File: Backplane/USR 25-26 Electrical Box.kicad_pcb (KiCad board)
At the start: 2 copper layers, 3 parts

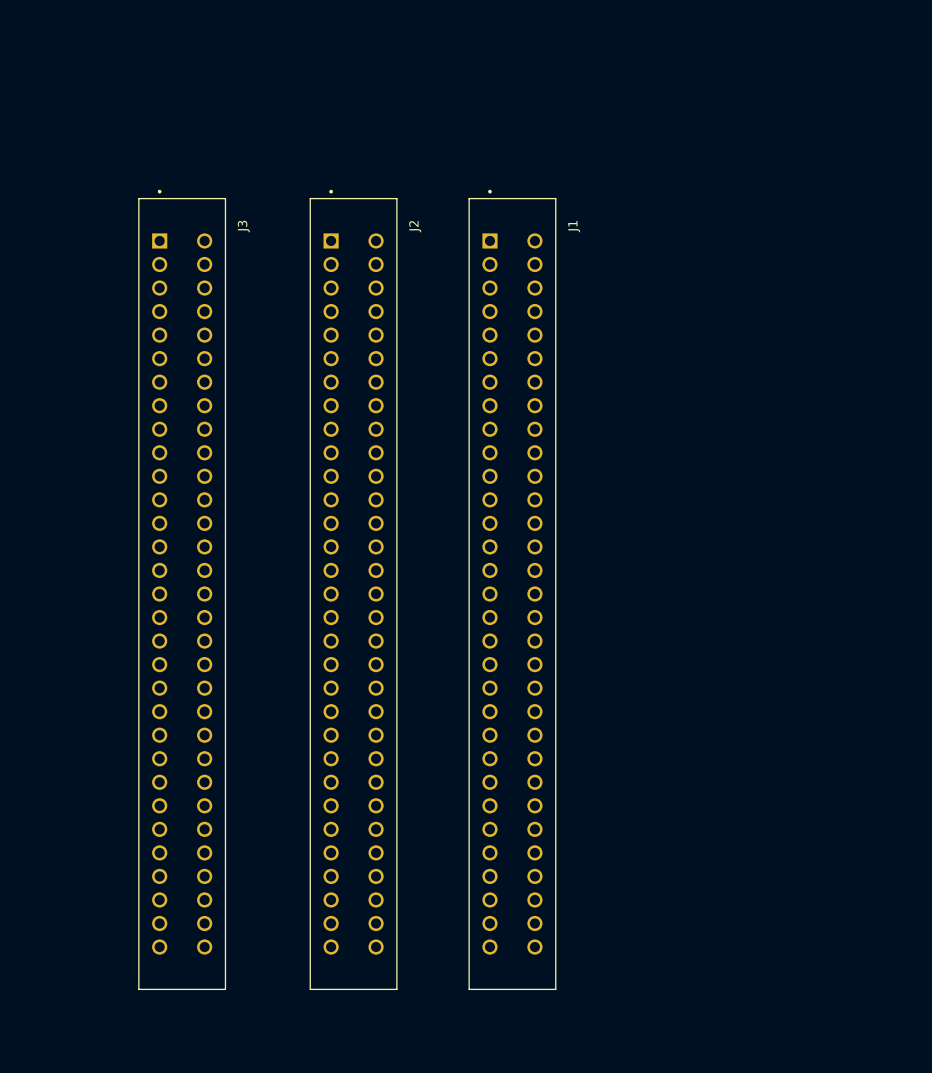
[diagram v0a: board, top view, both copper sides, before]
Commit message: Laid out revision 0 PCB for backplane.
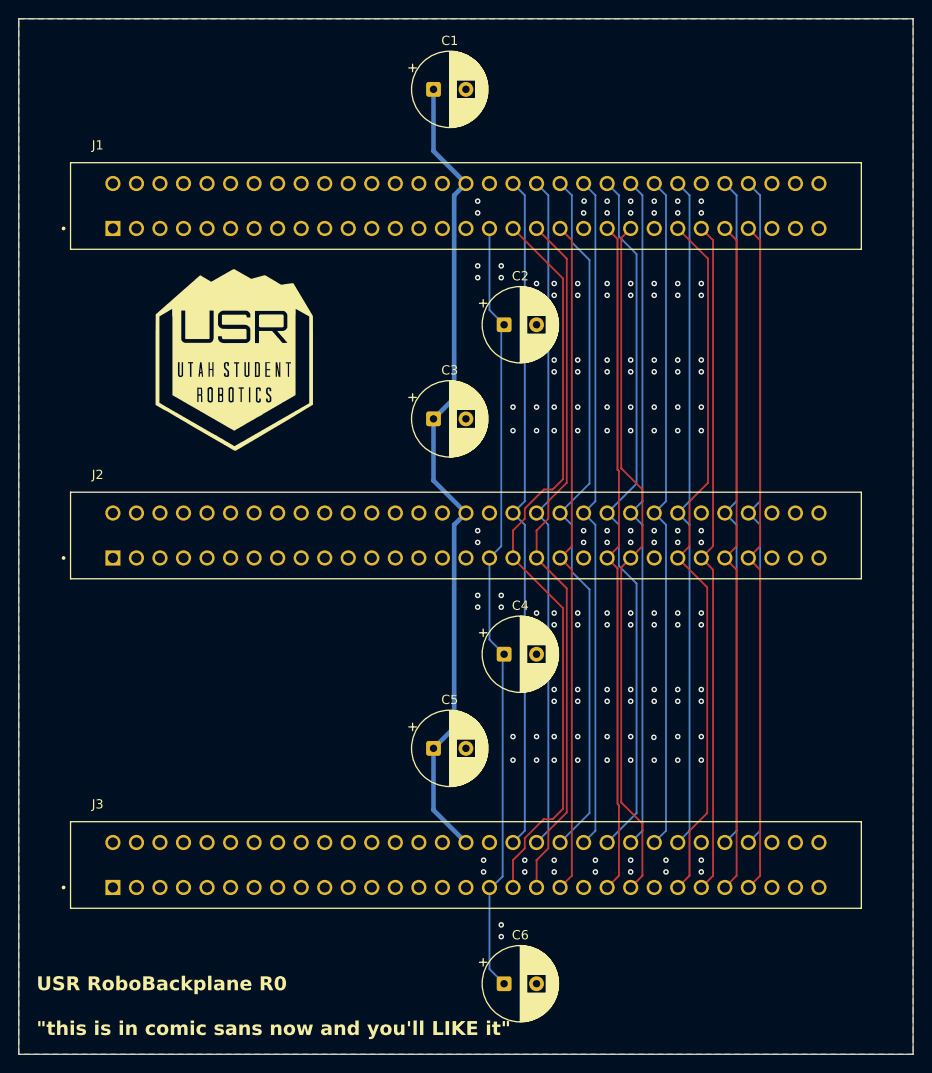
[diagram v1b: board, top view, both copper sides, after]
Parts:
- added C1: 100uF, Capacitor_THT:CP_Radial_D8.0mm_P3.50mm, F.Cu at (136.2, 40.6)
- added C2: 100uF, Capacitor_THT:CP_Radial_D8.0mm_P3.50mm, F.Cu at (143.8, 66.0)
- added C3: 100uF, Capacitor_THT:CP_Radial_D8.0mm_P3.50mm, F.Cu at (136.2, 76.2)
- added C4: 100uF, Capacitor_THT:CP_Radial_D8.0mm_P3.50mm, F.Cu at (143.8, 101.6)
- added C5: 100uF, Capacitor_THT:CP_Radial_D8.0mm_P3.50mm, F.Cu at (136.2, 111.8)
- added C6: 100uF, Capacitor_THT:CP_Radial_D8.0mm_P3.50mm, F.Cu at (143.8, 137.2)
- moved J3 42.3 mm to (139.7, 124.3), turned to 0 degrees
- moved J1 42.2 mm to (139.7, 53.2), turned to 0 degrees
- moved J2 13.7 mm to (139.7, 88.8), turned to 0 degrees
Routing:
- net +5V: track 0.00 -> 88.5 mm
- net +3V3: track 0.00 -> 85.0 mm
- net SPI0_MOSI: track 0.00 -> 81.2 mm
- net SPI0_SCLK: track 0.00 -> 76.5 mm
- net M1_FLT: track 0.00 -> 76.5 mm
- net SPI1_SCLK: track 0.00 -> 76.4 mm
- net SPI0_CS2: track 0.00 -> 76.4 mm
- net SPI1_CS0: track 0.00 -> 74.9 mm
- net SPI1_MISO: track 0.00 -> 73.2 mm
- net SPI1_CS1: track 0.00 -> 73.2 mm
- net SPI0_MISO: track 0.00 -> 73.2 mm
- net SPI0_CS0: track 0.00 -> 73.2 mm
- net M2_FLT: track 0.00 -> 73.2 mm
- net M2_DIR: track 0.00 -> 73.2 mm
- net M1_SLP: track 0.00 -> 73.2 mm
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- added copper zone on B.Cu, net GND
- added copper zone on F.Cu, net GND
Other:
- board outline added: 96.5 x 111.8 mm
- board text added: "USR RoboBackplane R0 {dblquote}this is in comic sans now and you'll LIKE it{dblquote}"
